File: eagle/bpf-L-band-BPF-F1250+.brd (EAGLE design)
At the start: 48 x 27 mm, 3 parts, among them J1 142-0701-851, J2 142-0701-851, U1 BPF-F1250+

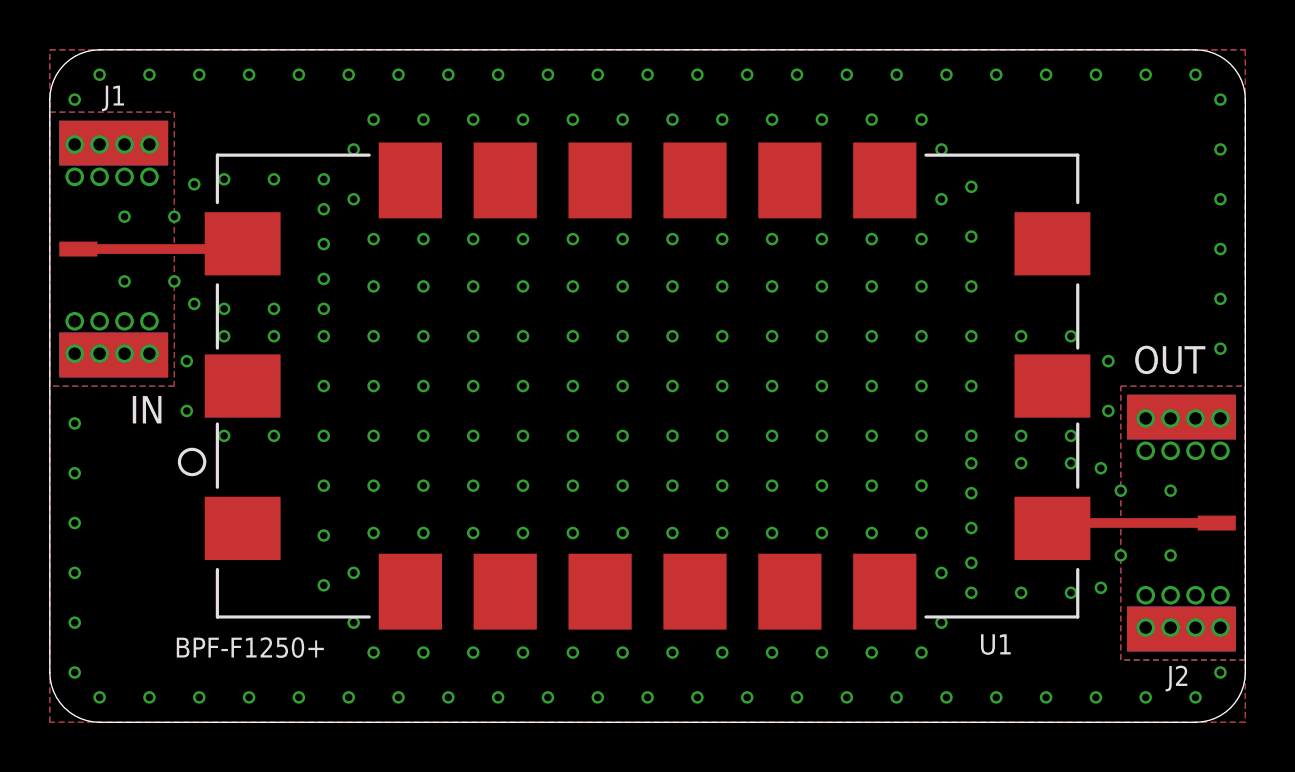
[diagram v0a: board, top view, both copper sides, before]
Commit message: Changed MiniCirc BPFs to 2-layer and adjusted for CBCPW
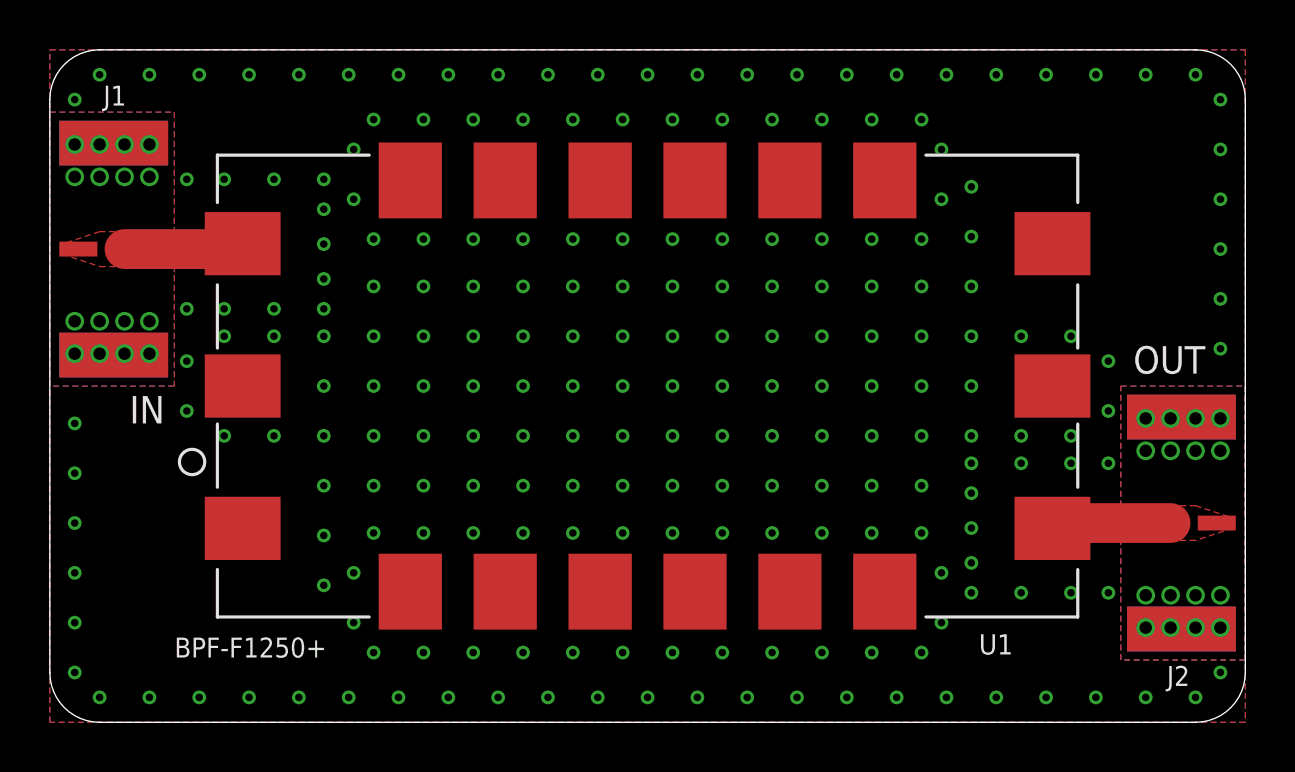
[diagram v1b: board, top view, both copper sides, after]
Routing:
- net RF-OUT: track 6.69 -> 5.14 mm
- net RF-IN: track 6.69 -> 5.14 mm
- added copper zone on layer 1, net RF-IN
- added copper zone on layer 1, net RF-OUT
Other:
- board text added: "L band BPF-F1250+ PSAS / OreSat 2019-09-28 v1 E.M. KJ7AOG"
- board text removed: "L band BPF-F1250+ PSAS / OreSat 2019-09-25 v1 E.M. KJ7AOG"
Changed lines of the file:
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@@
 <drawing>
 <settings>
-<setting alwaysvectorfont="no"/>
+<setting alwaysvectorfont="yes"/>
 <setting verticaltext="up"/>
 </settings>
@@
 <wire x1="48" y1="2" x2="48" y2="25" width="0" layer="20"/>
 <wire x1="48" y1="25" x2="46" y2="27" width="0" layer="20" curve="90"/>
-<wire x1="0" y1="19" x2="4.9" y2="19" width="2" layer="29"/>
-<wire x1="48" y1="8" x2="43.1" y2="8" width="2" layer="29"/>
+<wire x1="0" y1="19" x2="7" y2="19" width="2.4" layer="29"/>
+<wire x1="48" y1="8" x2="40.9" y2="8" width="2.4" layer="29"/>
 <wire x1="0" y1="19" x2="3" y2="19" width="2" layer="30"/>
 <wire x1="48" y1="8" x2="45" y2="8" width="2" layer="30"/>
@@
 <text x="31" y="12" size="1.3" layer="22" font="vector" ratio="15" rot="MR0">L band BPF-F1250+
 PSAS / OreSat
-2019-09-25  v1
+2019-09-28  v1
 E.M.  KJ7AOG</text>
 <text x="5" y="2.6" size="0.8" layer="21" font="vector" ratio="15">BPF-F1250+</text>
@@
 </class>
 <class number="1" name="RF" width="0" drill="0">
-<clearance class="1" value="0.8"/>
+<clearance class="1" value="0.31"/>
 </class>
 </classes>
-<designrules name="oshpark-4layer-tented">
+<designrules name="oshpark-2layer-tented">
 <description language="en">&lt;b&gt;OSH Park Design Rules&lt;/b&gt;
 &lt;p&gt;
@@
 &lt;a href=&quot;http://docs.oshpark.com/design-tools/eagle/design-rules-files/&quot;&gt;Adjustable Settings&lt;/a&gt;
 &lt;/p&gt;</description>
-<param name="layerSetup" value="(1*2*15*16)"/>
-<param name="mtCopper" value="0.035559375mm 0.01778125mm 0.0356mm 0.0356mm 0.0356mm 0.0356mm 0.0356mm 0.0356mm 0.0356mm 0.0356mm 0.0356mm 0.0356mm 0.0356mm 0.0356mm 0.01778125mm 0.035559375mm"/>
-<param name="mtIsolate" value="0.17018125mm 47mil 0.2007mm 0.1499mm 0.2007mm 0.1499mm 0.2007mm 0.1499mm 0.2007mm 0.1499mm 0.2007mm 0.1499mm 0.2007mm 0.1499mm 0.17018125mm"/>
-<param name="mdWireWire" value="5mil"/>
-<param name="mdWirePad" value="5mil"/>
-<param name="mdWireVia" value="5mil"/>
-<param name="mdPadPad" value="5mil"/>
-<param name="mdPadVia" value="5mil"/>
-<param name="mdViaVia" value="5mil"/>
-<param name="mdSmdPad" value="5mil"/>
-<param name="mdSmdVia" value="5mil"/>
-<param name="mdSmdSmd" value="5mil"/>
+<param name="layerSetup" value="(1*16)"/>
+<param name="mtCopper" value="0.035559375mm 0.0356mm 0.0356mm 0.0356mm 0.0356mm 0.0356mm 0.0356mm 0.0356mm 0.0356mm 0.0356mm 0.0356mm 0.0356mm 0.0356mm 0.0356mm 0.0356mm 0.035559375mm"/>
+<param name="mtIsolate" value="1.6mm 0.1499mm 0.2007mm 0.1499mm 0.2007mm 0.1499mm 0.2007mm 0.1499mm 0.2007mm 0.1499mm 0.2007mm 0.1499mm 0.2007mm 0.1499mm 0.2007mm"/>
+<param name="mdWireWire" value="6mil"/>
+<param name="mdWirePad" value="6mil"/>
+<param name="mdWireVia" value="6mil"/>
+<param name="mdPadPad" value="6mil"/>
+<param name="mdPadVia" value="6mil"/>
+<param name="mdViaVia" value="6mil"/>
+<param name="mdSmdPad" value="6mil"/>
+<param name="mdSmdVia" value="6mil"/>
+<param name="mdSmdSmd" value="6mil"/>
 <param name="mdViaViaSameLayer" value="8mil"/>
 <param name="mnLayersViaInSmd" value="2"/>
@@
 <param name="mdDrill" value="6mil"/>
 <param name="mdSmdStop" value="0mil"/>
-<param name="msWidth" value="5mil"/>
+<param name="msWidth" value="6mil"/>
 <param name="msDrill" value="10mil"/>
 <param name="msMicroVia" value="10mil"/>
@@
 <param name="rvMicroViaOuter" value="0.25"/>
 <param name="rvMicroViaInner" value="0.25"/>
-<param name="rlMinPadTop" value="4mil"/>
+<param name="rlMinPadTop" value="5mil"/>
 <param name="rlMaxPadTop" value="20mil"/>
-<param name="rlMinPadInner" value="4mil"/>
+<param name="rlMinPadInner" value="5mil"/>
 <param name="rlMaxPadInner" value="20mil"/>
-<param name="rlMinPadBottom" value="4mil"/>
+<param name="rlMinPadBottom" value="5mil"/>
 <param name="rlMaxPadBottom" value="20mil"/>
-<param name="rlMinViaOuter" value="4mil"/>
+<param name="rlMinViaOuter" value="5mil"/>
 <param name="rlMaxViaOuter" value="20mil"/>
-<param name="rlMinViaInner" value="4mil"/>
+<param name="rlMinViaInner" value="5mil"/>
 <param name="rlMaxViaInner" value="20mil"/>
-<param name="rlMinMicroViaOuter" value="4mil"/>
+<param name="rlMinMicroViaOuter" value="5mil"/>
 <param name="rlMaxMicroViaOuter" value="20mil"/>
-<param name="rlMinMicroViaInner" value="4mil"/>
+<param name="rlMinMicroViaInner" value="5mil"/>
 <param name="rlMaxMicroViaInner" value="20mil"/>
 <param name="psTop" value="-1"/>
@@
 <contactref element="J2" pad="GND3"/>
 <contactref element="J2" pad="GND4"/>
-<polygon width="0.3" layer="1">
+<polygon width="0.3" layer="1" rank="2">
 <vertex x="0" y="27"/>
 <vertex x="48" y="27"/>
@@
 <vertex x="0" y="0"/>
 </polygon>
-<polygon width="0.3" layer="1" thermals="no">
+<polygon width="0.3" layer="1" thermals="no" rank="2">
 <vertex x="0" y="24.5"/>
 <vertex x="5" y="24.5"/>
@@
 <vertex x="0" y="13.5"/>
 </polygon>
-<polygon width="0.3" layer="1" thermals="no">
+<polygon width="0.3" layer="1" thermals="no" rank="2">
 <vertex x="43" y="13.5"/>
 <vertex x="48" y="13.5"/>
@@
 <via x="46" y="10.9" extent="1-16" drill="0.5"/>
 <via x="47" y="10.9" extent="1-16" drill="0.5"/>
-<via x="3" y="17.7" extent="1-16" drill="0.3"/>
-<via x="5" y="17.7" extent="1-16" drill="0.3"/>
-<via x="3" y="20.3" extent="1-16" drill="0.3"/>
-<via x="5" y="20.3" extent="1-16" drill="0.3"/>
-<via x="45" y="6.7" extent="1-16" drill="0.3"/>
-<via x="45" y="9.3" extent="1-16" drill="0.3"/>
-<via x="43" y="9.3" extent="1-16" drill="0.3"/>
-<via x="43" y="6.7" extent="1-16" drill="0.3"/>
 <via x="1" y="2" extent="1-16" drill="0.3"/>
 <via x="2" y="1" extent="1-16" drill="0.3"/>
@@
 <via x="11" y="21.8" extent="1-16" drill="0.3"/>
 <via x="7" y="21.8" extent="1-16" drill="0.3"/>
-<via x="5.8" y="21.6" extent="1-16" drill="0.3"/>
+<via x="5.5" y="21.8" extent="1-16" drill="0.3"/>
 <via x="7" y="16.6" extent="1-16" drill="0.3"/>
 <via x="9" y="16.6" extent="1-16" drill="0.3"/>
@@
 <via x="39" y="10.4" extent="1-16" drill="0.3"/>
 <via x="41" y="10.4" extent="1-16" drill="0.3"/>
-<via x="42.2" y="10.2" extent="1-16" drill="0.3"/>
+<via x="42.5" y="10.4" extent="1-16" drill="0.3"/>
 <via x="37" y="5.2" extent="1-16" drill="0.3"/>
 <via x="39" y="5.2" extent="1-16" drill="0.3"/>
 <via x="41" y="5.2" extent="1-16" drill="0.3"/>
-<via x="42.2" y="5.4" extent="1-16" drill="0.3"/>
-<via x="5.8" y="16.8" extent="1-16" drill="0.3"/>
+<via x="42.5" y="5.2" extent="1-16" drill="0.3"/>
+<via x="5.5" y="16.6" extent="1-16" drill="0.3"/>
 <via x="13" y="2.8" extent="1-16" drill="0.3"/>
 <via x="15" y="2.8" extent="1-16" drill="0.3"/>
@@
 <contactref element="J1" pad="RF1"/>
 <contactref element="U1" pad="18"/>
-<wire x1="1.146" y1="19" x2="7.529" y2="19" width="0.39" layer="1"/>
 <wire x1="7.529" y1="19" x2="7.744" y2="19.215" width="0.39" layer="1"/>
+<wire x1="7.744" y1="19.215" x2="7.529" y2="19" width="1.6" layer="1"/>
+<wire x1="7.529" y1="19" x2="3" y2="19" width="1.6" layer="1"/>
+<polygon width="0.2" layer="1" thermals="no">
+<vertex x="3" y="19.7"/>
+<vertex x="2" y="19.7"/>
+<vertex x="0.5" y="19.2"/>
+<vertex x="0.5" y="18.8"/>
+<vertex x="2" y="18.3"/>
+<vertex x="3" y="18.3"/>
+</polygon>
 </signal>
 <signal name="RF-OUT" class="1">
 <contactref element="J2" pad="RF1"/>
 <contactref element="U1" pad="9"/>
-<wire x1="46.854" y1="8" x2="40.471" y2="8" width="0.39" layer="1"/>
 <wire x1="40.471" y1="8" x2="40.256" y2="7.785" width="0.39" layer="1"/>
+<wire x1="40.256" y1="7.785" x2="40.471" y2="8" width="1.6" layer="1"/>
+<wire x1="40.471" y1="8" x2="45" y2="8" width="1.6" layer="1"/>
+<polygon width="0.2" layer="1" thermals="no">
+<vertex x="45" y="8.7"/>
+<vertex x="46" y="8.7"/>
+<vertex x="47.5" y="8.2"/>
+<vertex x="47.5" y="7.8"/>
+<vertex x="46" y="7.3"/>
+<vertex x="45" y="7.3"/>
+</polygon>
 </signal>
 </signals>
@@
 <mfgpreviewcolor name="substratecolor" color="0xFF786E46"/>
 </mfgpreviewcolors>
-<errors>
-</errors>
 </board>
 </drawing>
